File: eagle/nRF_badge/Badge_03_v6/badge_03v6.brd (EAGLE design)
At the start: 30 x 70 mm, 43 parts, among them U1 LIS2DH12, U2 LP2985LV, U3 MCP6231, U5 M95M02, Y1 32768Hz

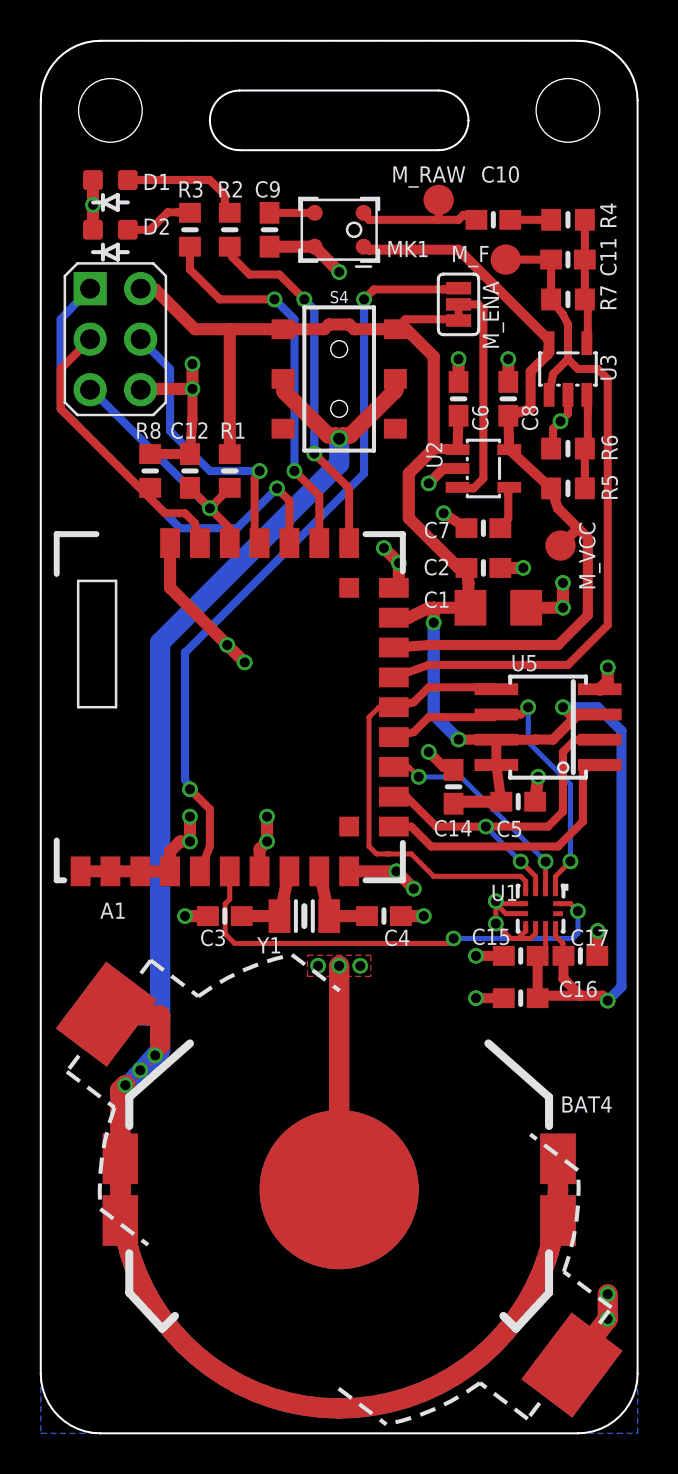
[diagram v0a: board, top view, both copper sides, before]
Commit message: change component for comliant design with technical note TN0018
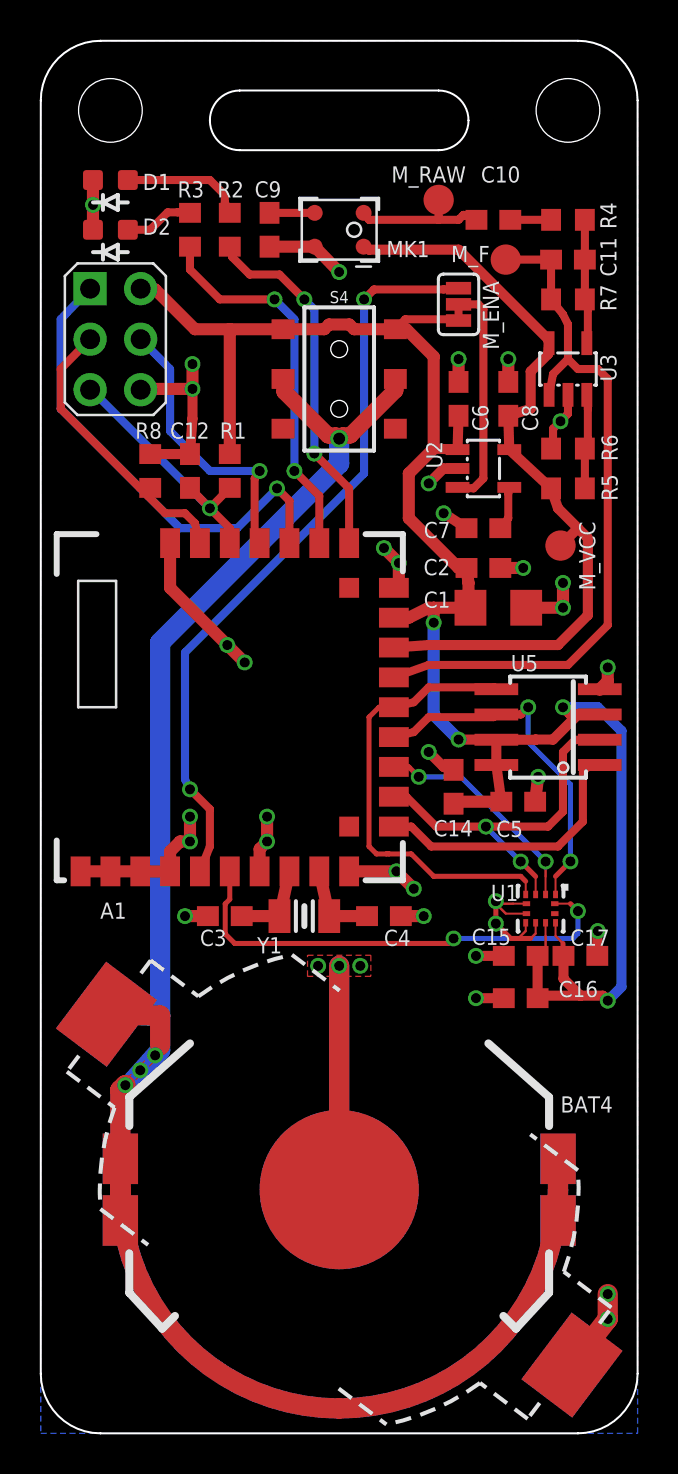
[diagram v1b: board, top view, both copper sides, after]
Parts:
- U1: device Badge:LGA12 -> st-microelectronics_modified:LGA12-TN0018-COMPLIANT
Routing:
- net GND: track 97.6 -> 98.3 mm

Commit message: Fix for issues generated in last commit, updated library
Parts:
- U1: value LIS2DH12 -> LIS2DH12"; device st-microelectronics_modified:LGA12-TN0018-COMPLIANT -> Badge:LGA12-TN0018-COMPLIANT
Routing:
- net VCC: track 98.9 -> 97.9 mm
- net VBATT: track 140.2 -> 140.7 mm

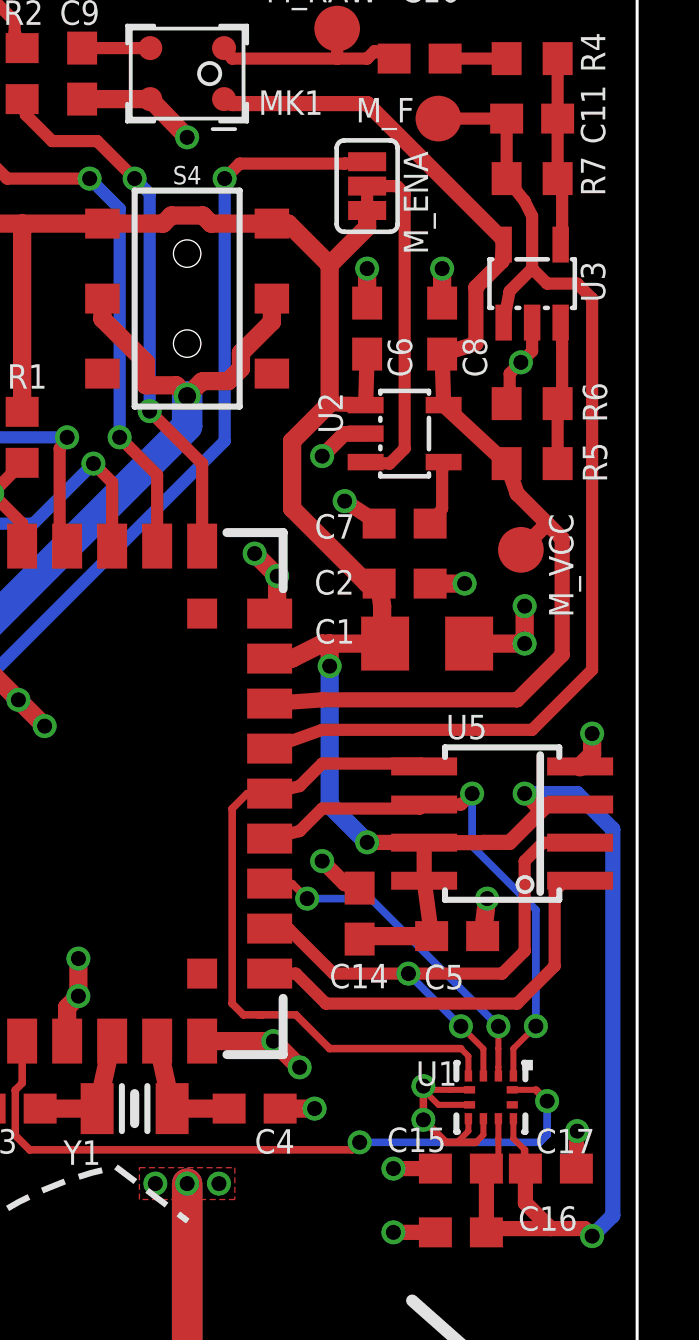
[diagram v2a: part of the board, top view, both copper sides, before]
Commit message: Approved Overlap in jumpar pad, errors is cause by DRC but package is fine.
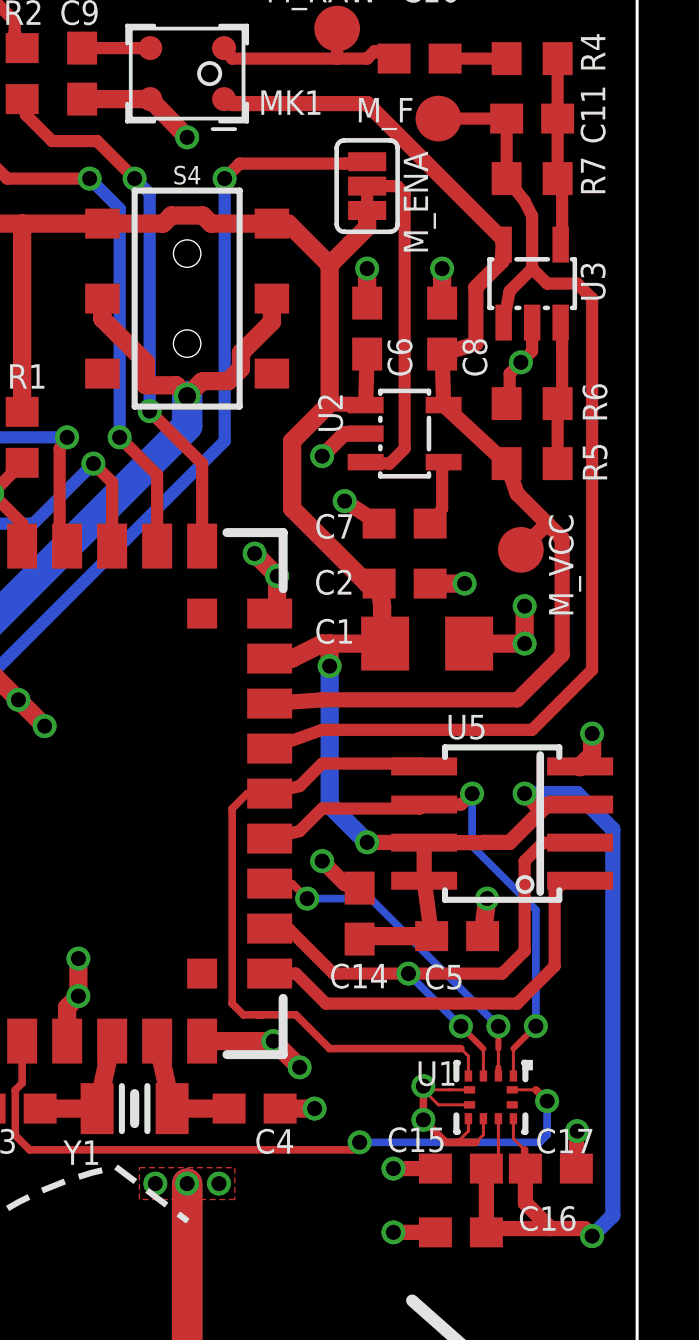
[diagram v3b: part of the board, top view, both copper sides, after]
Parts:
- M_ENA: value (none) -> JUMPER-PAD-3-2OF3_NC_BY_TRACE_SMALL
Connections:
- net N$6 renamed ON/OFF
- net N$9 renamed BYPASS
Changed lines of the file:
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@@
 </class>
 </classes>
-<designrules name="PCBNG_DRC_by_oren">
+<designrules name="PCBNG_DRC_by_oren *">
 <description language="de">&lt;b&gt;EAGLE Design Rules&lt;/b&gt;
 &lt;p&gt;
@@
 <param name="mdDrill" value="20mil"/>
 <param name="mdSmdStop" value="0mil"/>
-<param name="msWidth" value="6mil"/>
+<param name="msWidth" value="4mil"/>
 <param name="msDrill" value="12mil"/>
 <param name="msMicroVia" value="18mil"/>
@@
 <attribute name="VALUE" x="17.25" y="23.5" size="0.8128" layer="27" font="vector" ratio="16"/>
 </element>
-<element name="M_ENA" library="Badge" package="PAD-JUMPER-3-2OF3_NC_BY_TRACE_YES_SILK_FULL_BOX" value="" x="21" y="56.75" smashed="yes" rot="R270">
+<element name="M_ENA" library="Badge" package="PAD-JUMPER-3-2OF3_NC_BY_TRACE_YES_SILK_FULL_BOX" value="JUMPER-PAD-3-2OF3_NC_BY_TRACE_SMALL" x="21" y="56.75" smashed="yes" rot="R270">
 <attribute name="NAME" x="23.030971875" y="54.47120625" size="0.8128" layer="25" font="vector" ratio="16" rot="R90"/>
 </element>
@@
 <wire x1="23.275" y1="24" x2="21.875" y2="24" width="0.508" layer="1"/>
 <via x="21.875" y="24" extent="1-16" drill="0.5"/>
-<wire x1="24.875" y1="25.6625" x2="24.875" y2="25.125" width="0.2032" layer="1"/>
-<wire x1="24.875" y1="25.125" x2="24.625" y2="24.875" width="0.2032" layer="1"/>
+<wire x1="24.875" y1="25.6625" x2="24.875" y2="25.125" width="0.1016" layer="1"/>
+<wire x1="24.875" y1="25.125" x2="24.625" y2="24.875" width="0.1016" layer="1"/>
 <wire x1="24" y1="24.875" x2="24.625" y2="24.875" width="0.254" layer="1"/>
 <wire x1="24" y1="24.875" x2="23.625" y2="24.875" width="0.254" layer="1"/>
-<wire x1="24.375" y1="25.6625" x2="24.375" y2="25.25" width="0.2032" layer="1"/>
-<wire x1="24.375" y1="25.25" x2="24" y2="24.875" width="0.2032" layer="1"/>
+<wire x1="24.375" y1="25.6625" x2="24.375" y2="25.25" width="0.1016" layer="1"/>
+<wire x1="24.375" y1="25.25" x2="24" y2="24.875" width="0.1016" layer="1"/>
 <via x="22.875" y="26.75" extent="1-16" drill="0.5"/>
 <wire x1="22.875" y1="25.625" x2="23.625" y2="24.875" width="0.254" layer="1"/>
 <via x="22.875" y="25.625" extent="1-16" drill="0.5"/>
 <wire x1="23" y1="26.625" x2="22.875" y2="26.75" width="0.254" layer="1"/>
-<wire x1="23" y1="26.5" x2="23.375" y2="26.125" width="0.2032" layer="1"/>
+<wire x1="23" y1="26.5" x2="23.375" y2="26.125" width="0.1016" layer="1"/>
 <wire x1="23" y1="26.5" x2="23" y2="26.625" width="0.254" layer="1"/>
 <wire x1="22.875" y1="26.75" x2="22.875" y2="25.625" width="0.254" layer="1"/>
 <wire x1="28" y1="25.25" x2="27.975" y2="25.225" width="0.508" layer="1"/>
 <wire x1="27.975" y1="25.225" x2="27.975" y2="24" width="0.508" layer="1"/>
-<wire x1="23" y1="26.625" x2="23.75" y2="26.625" width="0.2032" layer="1"/>
-<wire x1="23.375" y1="26.125" x2="24.4125" y2="26.125" width="0.2032" layer="1"/>
-<wire x1="23.75" y1="26.625" x2="24.4125" y2="26.625" width="0.2032" layer="1"/>
+<wire x1="23" y1="26.625" x2="23.75" y2="26.625" width="0.1016" layer="1"/>
+<wire x1="23.375" y1="26.125" x2="24.4125" y2="26.125" width="0.1016" layer="1"/>
+<wire x1="23.75" y1="26.625" x2="24.4125" y2="26.625" width="0.1016" layer="1"/>
 </signal>
 <signal name="VCC">
@@
 <contactref element="C16" pad="1"/>
 <wire x1="28.5" y1="21.75" x2="28.25" y2="22" width="0.508" layer="1"/>
-<wire x1="25.875" y1="25.6625" x2="25.875" y2="25" width="0.2032" layer="1"/>
-<wire x1="25.875" y1="25" x2="26.25" y2="24.625" width="0.2032" layer="1"/>
+<wire x1="25.875" y1="25.6625" x2="25.875" y2="25" width="0.1016" layer="1"/>
+<wire x1="25.875" y1="25" x2="26.25" y2="24.625" width="0.1016" layer="1"/>
 <wire x1="26.25" y1="24.625" x2="26.25" y2="24.025" width="0.254" layer="1"/>
 <wire x1="26.25" y1="24.025" x2="26.275" y2="24" width="0.254" layer="1"/>
@@
 <wire x1="24.975" y1="22.125" x2="25.1" y2="22" width="0.508" layer="1"/>
 <wire x1="24.975" y1="24" x2="25.375" y2="24.375" width="0.254" layer="1"/>
-<wire x1="25.375" y1="24.375" x2="25.375" y2="25" width="0.2032" layer="1"/>
-<wire x1="25.375" y1="25" x2="25.375" y2="25.6625" width="0.2032" layer="1"/>
+<wire x1="25.375" y1="24.375" x2="25.375" y2="25.6625" width="0.1016" layer="1"/>
 <wire x1="12.175" y1="55.5" x2="14.20394375" y2="55.5" width="0.6096" layer="1"/>
 <wire x1="14.20394375" y1="55.5" x2="14.47394375" y2="55.77" width="0.6096" layer="1"/>
@@
 <via x="26.625" y="28.75" extent="1-16" drill="0.5" diameter="0.8"/>
 <wire x1="26.625" y1="28.75" x2="25.875" y2="28" width="0.2032" layer="1"/>
-<wire x1="25.875" y1="28" x2="25.875" y2="27.0875" width="0.2032" layer="1"/>
+<wire x1="25.875" y1="28" x2="25.875" y2="27.0875" width="0.1016" layer="1"/>
 </signal>
 <signal name="MIC_F">
@@
 <wire x1="6.875" y1="61.375" x2="7.5" y2="61.35" width="0.4064" layer="1"/>
 </signal>
-<signal name="N$6">
+<signal name="ON/OFF">
 <contactref element="U2" pad="3"/>
 <contactref element="M_ENA" pad="2"/>
@@
 <wire x1="17.5" y1="29.125" x2="18.625" y2="29.125" width="0.254" layer="1"/>
 <wire x1="18.625" y1="29.125" x2="19.75" y2="28" width="0.254" layer="1"/>
-<wire x1="24.125" y1="28" x2="24.375" y2="27.75" width="0.2032" layer="1"/>
-<wire x1="24.375" y1="27.75" x2="24.375" y2="27.0875" width="0.2032" layer="1"/>
+<wire x1="24.125" y1="28" x2="24.375" y2="27.75" width="0.1016" layer="1"/>
+<wire x1="24.375" y1="27.75" x2="24.375" y2="27.0875" width="0.1016" layer="1"/>
 <wire x1="19.75" y1="28" x2="24.125" y2="28" width="0.254" layer="1"/>
 </signal>
@@
 <via x="24.125" y="28.742" extent="1-16" drill="0.5" diameter="0.8"/>
 <wire x1="24.125" y1="28.742" x2="24.875" y2="27.992" width="0.2032" layer="1"/>
-<wire x1="24.875" y1="27.992" x2="24.875" y2="27.0875" width="0.2032" layer="1"/>
+<wire x1="24.875" y1="27.992" x2="24.875" y2="27.0875" width="0.1016" layer="1"/>
 <wire x1="24.125" y1="28.742" x2="22.375" y2="30.492" width="0.254" layer="16"/>
 <wire x1="22.375" y1="30.492" x2="22.375" y2="30.5" width="0.254" layer="16"/>
@@
 <wire x1="16.4" y1="26" x2="14.5" y2="26" width="0.6096" layer="1"/>
 </signal>
-<signal name="N$9">
+<signal name="BYPASS">
 <contactref element="U2" pad="4"/>
 <contactref element="C7" pad="2"/>
@@
 <contactref element="U1" pad="12"/>
 <contactref element="A1" pad="P$6"/>
-<wire x1="25.8375" y1="26.625" x2="26.625" y2="26.625" width="0.2032" layer="1"/>
+<wire x1="25.8375" y1="26.625" x2="26.625" y2="26.625" width="0.1016" layer="1"/>
 <wire x1="26.625" y1="26.625" x2="27" y2="26.25" width="0.254" layer="1"/>
 <via x="27" y="26.25" extent="1-16" drill="0.5" diameter="0.8"/>
@@
 <via x="25.375" y="28.742" extent="1-16" drill="0.5" diameter="0.8"/>
 <wire x1="25.375" y1="28.742" x2="25.375" y2="28" width="0.2032" layer="1"/>
-<wire x1="25.375" y1="28" x2="25.375" y2="27.375" width="0.2032" layer="1"/>
+<wire x1="25.375" y1="28" x2="25.375" y2="27.375" width="0.1016" layer="1"/>
 <wire x1="25.375" y1="27.375" x2="25.375" y2="27.0875" width="0.2032" layer="1"/>
 </signal>

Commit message: Updated DRC. Small fixed to board design
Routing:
- net VBATT: track 140.7 -> 139.6 mm
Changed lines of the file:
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@@
 </class>
 </classes>
-<designrules name="PCBNG_DRC_by_oren *">
+<designrules name="PCBNG_DRC_by_oren">
 <description language="de">&lt;b&gt;EAGLE Design Rules&lt;/b&gt;
 &lt;p&gt;
@@
 <contactref element="S4" pad="5"/>
 <wire x1="12.25" y1="53" x2="12.175" y2="53" width="0.6096" layer="1"/>
-<wire x1="12.175" y1="53" x2="12.175" y2="52.325" width="0.6096" layer="1"/>
-<wire x1="13.625" y1="50.875" x2="13.625" y2="50.1096" width="0.6096" layer="1"/>
-<wire x1="12.175" y1="52.325" x2="13.625" y2="50.875" width="0.6096" layer="1"/>
-<wire x1="13.625" y1="50.1096" x2="14.6404" y2="50.1096" width="0.6096" layer="1"/>
-<wire x1="14.6404" y1="50.1096" x2="15" y2="49.75" width="0.6096" layer="1"/>
 <wire x1="15" y1="49.75" x2="15.48" y2="50.23" width="0.6096" layer="1"/>
 <wire x1="15.48" y1="50.23" x2="15.52605625" y2="50.23" width="0.6096" layer="1"/>
-<wire x1="15.52605625" y1="50.23" x2="15.54605625" y2="50.25" width="0.6096" layer="1"/>
-<wire x1="15.54605625" y1="50.25" x2="16.375" y2="50.25" width="0.6096" layer="1"/>
-<wire x1="16.375" y1="50.25" x2="16.7928" y2="50.6678" width="0.6096" layer="1"/>
-<wire x1="16.7928" y1="50.6678" x2="16.7928" y2="51.18938125" width="0.6096" layer="1"/>
-<wire x1="17.825" y1="52.22158125" x2="17.825" y2="53" width="0.6096" layer="1"/>
-<wire x1="16.7928" y1="51.18938125" x2="17.825" y2="52.22158125" width="0.6096" layer="1"/>
+<wire x1="15.52605625" y1="50.23" x2="17.825" y2="52.52894375" width="0.6096" layer="1"/>
+<wire x1="17.825" y1="52.52894375" x2="17.825" y2="53" width="0.6096" layer="1"/>
+<wire x1="15" y1="49.75" x2="14.52" y2="50.23" width="0.6096" layer="1"/>
+<wire x1="14.52" y1="50.23" x2="14.47394375" y2="50.23" width="0.6096" layer="1"/>
+<wire x1="14.47394375" y1="50.23" x2="12.25" y2="52.45394375" width="0.6096" layer="1"/>
+<wire x1="12.25" y1="52.45394375" x2="12.25" y2="53" width="0.6096" layer="1"/>
 </signal>
 <signal name="MOSI">
@@
 <wire x1="25.375" y1="28.742" x2="25.375" y2="28" width="0.2032" layer="1"/>
 <wire x1="25.375" y1="28" x2="25.375" y2="27.375" width="0.1016" layer="1"/>
-<wire x1="25.375" y1="27.375" x2="25.375" y2="27.0875" width="0.2032" layer="1"/>
+<wire x1="25.375" y1="27.375" x2="25.375" y2="27.0875" width="0.1016" layer="1"/>
 </signal>
 </signals>
